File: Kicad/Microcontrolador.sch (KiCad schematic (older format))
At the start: 1 part, among them U1 MSP430G2231IPW14

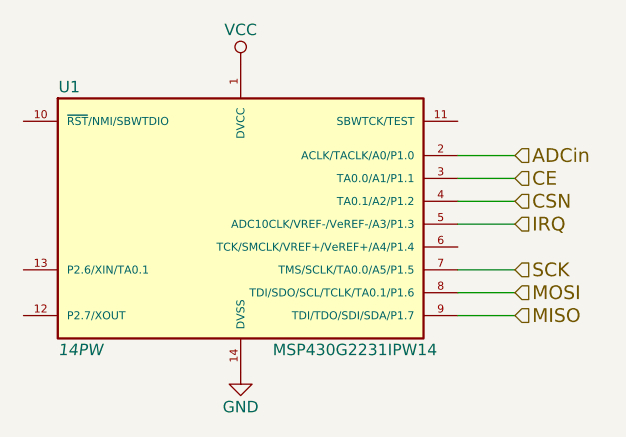
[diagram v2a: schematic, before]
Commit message: Circuito de cargador modificado. A los demás les agregué capacitor en la alimentación, pines sin conexión y cambié BATT- por GND
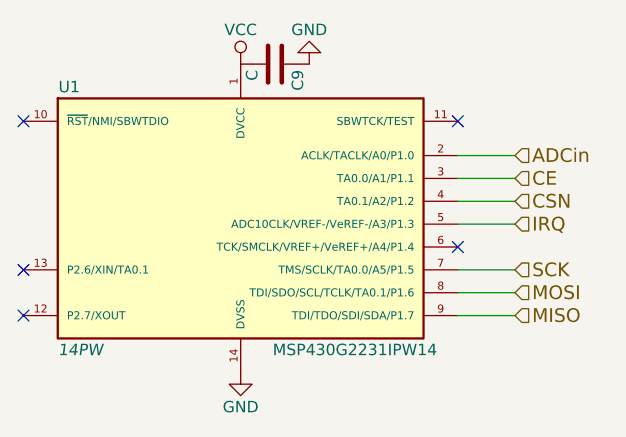
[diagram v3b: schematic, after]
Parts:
- added C9: C, symbol C
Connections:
- net GND: now also C9.1
- net VCC: now also C9.2
- no-connect marks 0 -> 5
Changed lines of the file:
@@
 Wire Wire Line
 	6350 3600 6600 3600
+$Comp
+L GND #PWR11
+U 1 1 57FAAB35
+P 5700 2500
+F 0 "#PWR11" H 5700 2250 50  0001 C CNN
+F 1 "GND" H 5700 2350 50  0000 C CNN
+F 2 "" H 5700 2500 50  0000 C CNN
+F 3 "" H 5700 2500 50  0000 C CNN
+	1    5700 2500
+	-1   0    0    1
+$EndComp
+$Comp
+L C C9
+U 1 1 57FAAB67
+P 5550 2500
+F 0 "C9" H 5575 2600 50  0000 L CNN
+F 1 "C" H 5575 2400 50  0000 L CNN
+F 2 "" H 5588 2350 50  0000 C CNN
+F 3 "" H 5550 2500 50  0000 C CNN
+	1    5550 2500
+	0    1    1    0
+$EndComp
+NoConn ~ 4450 2750
+NoConn ~ 4450 3400
+NoConn ~ 4450 3600
+NoConn ~ 6350 2750
+NoConn ~ 6350 3300
 $EndSCHEMATC

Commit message: Agregados footprints y 3D de SOT23-6. Asociado componente IC1
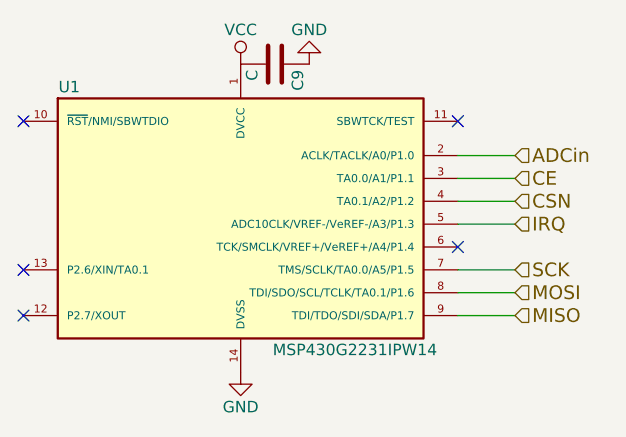
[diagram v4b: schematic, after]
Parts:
- U1: footprint 14PW -> (none)
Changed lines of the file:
@@
 F 0 "U1" H 4650 3800 50  0000 C CNN
 F 1 "MSP430G2231IPW14" H 5900 2650 50  0000 C CNN
-F 2 "14PW" H 4700 2650 50  0000 C CIN
+F 2 "" H 4700 2650 50  0000 C CIN
 F 3 "" H 5400 3200 50  0000 C CNN
 	1    5400 3200
@@
 $EndComp
 $Comp
-L VCC #PWR9
+L VCC #PWR09
 U 1 1 57DD89FE
 P 5400 2500
-F 0 "#PWR9" H 5400 2350 50  0001 C CNN
+F 0 "#PWR09" H 5400 2350 50  0001 C CNN
 F 1 "VCC" H 5400 2650 50  0000 C CNN
 F 2 "" H 5400 2500 50  0000 C CNN
@@
 $EndComp
 $Comp
-L GND #PWR10
+L GND #PWR010
 U 1 1 57DD8A14
 P 5400 3850
-F 0 "#PWR10" H 5400 3600 50  0001 C CNN
+F 0 "#PWR010" H 5400 3600 50  0001 C CNN
 F 1 "GND" H 5400 3700 50  0000 C CNN
 F 2 "" H 5400 3850 50  0000 C CNN
@@
 	6350 3600 6600 3600
 $Comp
-L GND #PWR11
+L GND #PWR011
 U 1 1 57FAAB35
 P 5700 2500
-F 0 "#PWR11" H 5700 2250 50  0001 C CNN
+F 0 "#PWR011" H 5700 2250 50  0001 C CNN
 F 1 "GND" H 5700 2350 50  0000 C CNN
 F 2 "" H 5700 2500 50  0000 C CNN
@@
 F 0 "C9" H 5575 2600 50  0000 L CNN
 F 1 "C" H 5575 2400 50  0000 L CNN
-F 2 "" H 5588 2350 50  0000 C CNN
+F 2 "" H 5588 2350 50  0001 C CNN
 F 3 "" H 5550 2500 50  0000 C CNN
 	1    5550 2500

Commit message: Agregados footprints de C_0805 y R_0805 y asociados a resistencias y capacitores del esquemático
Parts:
- C9: footprint (none) -> EMG:C_0805
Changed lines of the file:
@@
 F 0 "C9" H 5575 2600 50  0000 L CNN
 F 1 "C" H 5575 2400 50  0000 L CNN
-F 2 "" H 5588 2350 50  0001 C CNN
+F 2 "EMG:C_0805" H 5588 2350 50  0001 C CNN
 F 3 "" H 5550 2500 50  0000 C CNN
 	1    5550 2500

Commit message: Asociado footprint de msp430
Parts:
- U1: footprint (none) -> EMG:TSSOP-14_4.4x5mm_Pitch0.65mm
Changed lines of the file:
@@
 F 0 "U1" H 4650 3800 50  0000 C CNN
 F 1 "MSP430G2231IPW14" H 5900 2650 50  0000 C CNN
-F 2 "" H 4700 2650 50  0001 C CIN
+F 2 "EMG:TSSOP-14_4.4x5mm_Pitch0.65mm" H 4700 2650 50  0001 C CIN
 F 3 "" H 5400 3200 50  0000 C CNN
 	1    5400 3200
